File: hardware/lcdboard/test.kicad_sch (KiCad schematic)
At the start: 29 parts, among them J1 Conn_02x16_Odd_Even_MountingP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, J2 Conn_01x45_Shielded, J3 CapTouch, U1 74CBTLV3257, U2 AP2502

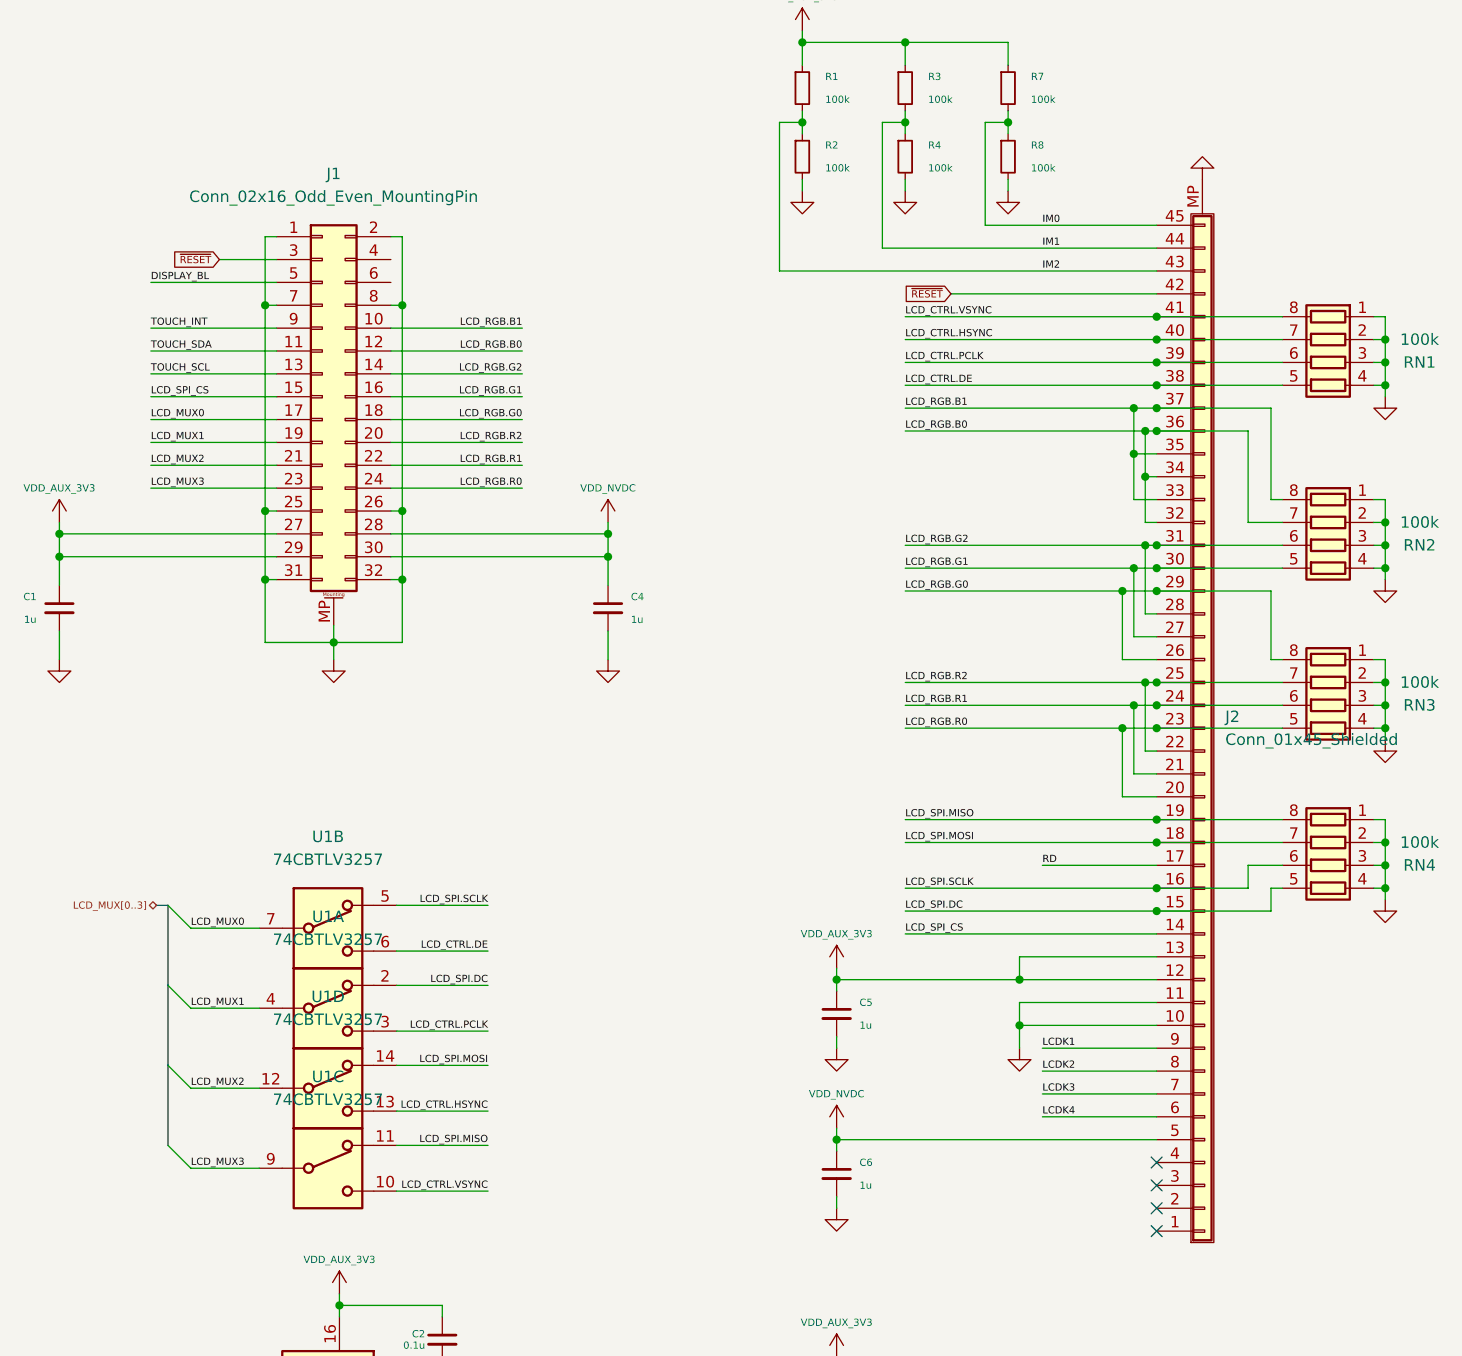
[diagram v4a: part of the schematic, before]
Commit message: completed layout for lcdboard prototype, may need to move b2b down for clearance on mainboard.
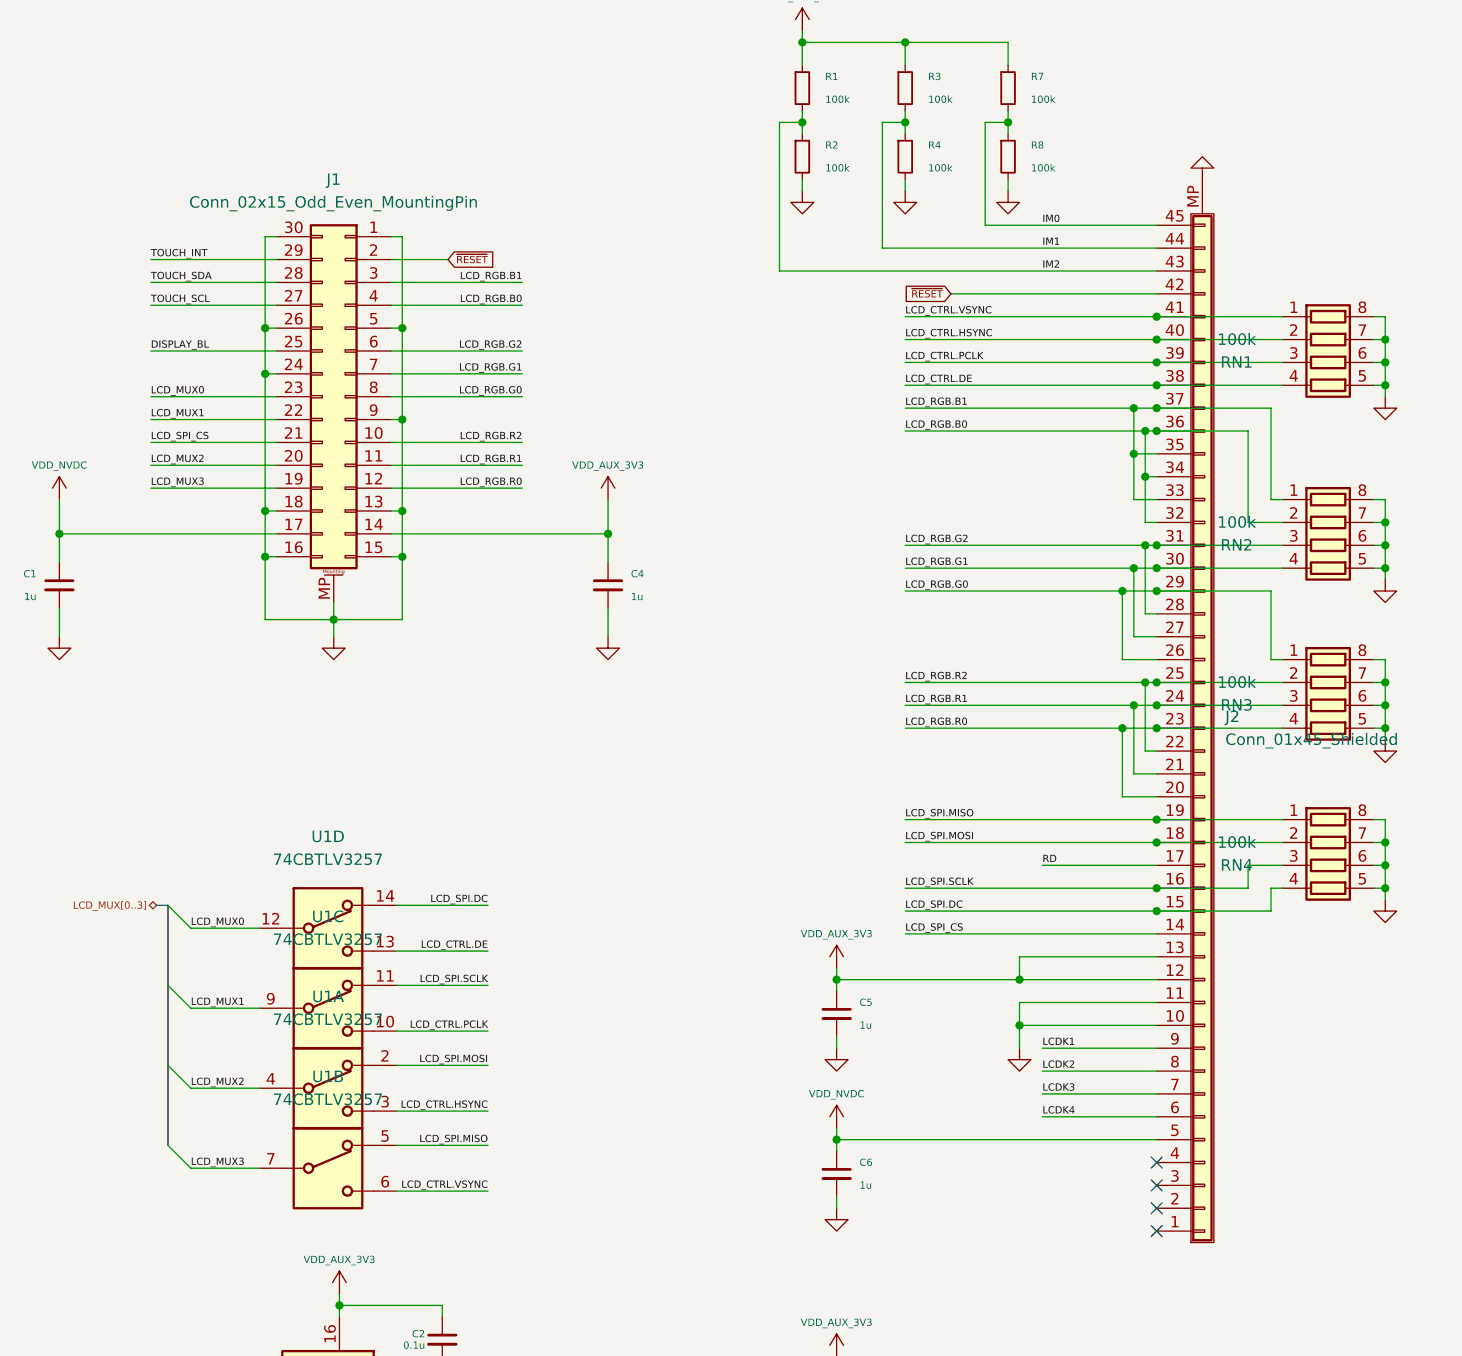
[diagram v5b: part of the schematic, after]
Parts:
- J1: value Conn_02x16_Odd_Even_MountingPin -> Conn_02x15_Odd_Even_MountingPin; footprint Connector_Molex:Molex_SlimStack_502426-3210_2x16_P0.40mm_Vertical -> bt_Connector_B2B:10132798-031100LF; symbol Connector_Generic_MountingPin:Conn_02x16_Odd_Even_MountingPin -> Connector_Generic_MountingPin:Conn_02x15_Counter_Clockwise_MountingPin
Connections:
- net DISPLAY_BL: now also J1.25 (Pin_25); no longer J1.5 (Pin_5)
- net GND: now also J1.13 (Pin_13), J1.15 (Pin_15), J1.16 (Pin_16), J1.18 (Pin_18), J1.24 (Pin_24), J1.30 (Pin_30), J1.5 (Pin_5), J1.9 (Pin_9), RN1.5 (R4.2), RN1.6 (R3.2), RN1.7 (R2.2), RN1.8 (R1.2), RN2.5 (R4.2), RN2.6 (R3.2), RN2.7 (R2.2), RN2.8 (R1.2), RN3.5 (R4.2), RN3.6 (R3.2), RN3.7 (R2.2), RN3.8 (R1.2), RN4.5 (R4.2), RN4.6 (R3.2), RN4.7 (R2.2), RN4.8 (R1.2); no longer J1.2 (Pin_2), J1.25 (Pin_25), J1.31 (Pin_31), J1.32 (Pin_32), J1.7 (Pin_7), J1.8 (Pin_8), RN1.1 (R1.1), RN1.2 (R2.1), RN1.3 (R3.1), RN1.4 (R4.1), RN2.1 (R1.1), RN2.2 (R2.1), RN2.3 (R3.1), RN2.4 (R4.1), RN3.1 (R1.1), RN3.2 (R2.1), RN3.3 (R3.1), RN3.4 (R4.1), RN4.1 (R1.1), RN4.2 (R2.1), RN4.3 (R3.1), RN4.4 (R4.1)
- net LCD_CTRL.DE: now also RN1.4 (R4.1), U1.13; no longer RN1.5 (R4.2), U1.6
- net LCD_CTRL.HSYNC: now also RN1.2 (R2.1), U1.3; no longer RN1.7 (R2.2), U1.13
- net LCD_CTRL.PCLK: now also RN1.3 (R3.1), U1.10; no longer RN1.6 (R3.2), U1.3
- net LCD_CTRL.VSYNC: now also RN1.1 (R1.1), U1.6; no longer RN1.8 (R1.2), U1.10
- net LCD_MUX0: now also J1.23 (Pin_23), U1.12; no longer J1.17 (Pin_17), U1.7
- net LCD_MUX1: now also J1.22 (Pin_22), U1.9; no longer J1.19 (Pin_19), U1.4
- net LCD_MUX2: now also J1.20 (Pin_20), U1.4; no longer J1.21 (Pin_21), U1.12
- net LCD_MUX3: now also J1.19 (Pin_19), U1.7; no longer J1.23 (Pin_23), U1.9
- net LCD_RGB.B0: now also J1.4 (Pin_4), RN2.2 (R2.1); no longer J1.12 (Pin_12), RN2.7 (R2.2)
- net LCD_RGB.B1: now also J1.3 (Pin_3), RN2.1 (R1.1); no longer J1.10 (Pin_10), RN2.8 (R1.2)
- net LCD_RGB.G0: now also J1.8 (Pin_8), RN3.1 (R1.1); no longer J1.18 (Pin_18), RN3.8 (R1.2)
- net LCD_RGB.G1: now also J1.7 (Pin_7), RN2.4 (R4.1); no longer J1.16 (Pin_16), RN2.5 (R4.2)
- net LCD_RGB.G2: now also J1.6 (Pin_6), RN2.3 (R3.1); no longer J1.14 (Pin_14), RN2.6 (R3.2)
- net LCD_RGB.R0: now also J1.12 (Pin_12), RN3.4 (R4.1); no longer J1.24 (Pin_24), RN3.5 (R4.2)
- net LCD_RGB.R1: now also J1.11 (Pin_11), RN3.3 (R3.1); no longer J1.22 (Pin_22), RN3.6 (R3.2)
- net LCD_RGB.R2: now also J1.10 (Pin_10), RN3.2 (R2.1); no longer J1.20 (Pin_20), RN3.7 (R2.2)
- net LCD_SPI.DC: now also RN4.4 (R4.1), U1.14; no longer RN4.5 (R4.2), U1.2
- net LCD_SPI.MISO: now also RN4.1 (R1.1), U1.5; no longer RN4.8 (R1.2), U1.11
- net LCD_SPI.MOSI: now also RN4.2 (R2.1), U1.2; no longer RN4.7 (R2.2), U1.14
- net LCD_SPI.SCLK: now also RN4.3 (R3.1), U1.11; no longer RN4.6 (R3.2), U1.5
- net LCD_SPI_CS: now also J1.21 (Pin_21); no longer J1.15 (Pin_15)
- net TOUCH_INT: now also J1.29 (Pin_29); no longer J1.9 (Pin_9)
- net TOUCH_SCL: now also J1.27 (Pin_27); no longer J1.13 (Pin_13)
- net TOUCH_SDA: now also J1.28 (Pin_28); no longer J1.11 (Pin_11)
- net VDD_AUX_3V3: now also C4.1, J1.14 (Pin_14); no longer C1.1, J1.27 (Pin_27), J1.29 (Pin_29)
- net VDD_NVDC: now also C1.1, J1.17 (Pin_17); no longer C4.1, J1.28 (Pin_28), J1.30 (Pin_30)
- net ~{RESET}: now also J1.2 (Pin_2); no longer J1.3 (Pin_3)
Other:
- moved on the sheet: C1, C4, RN1, RN2, RN3, RN4, U1A, U1B, U1C, U1D

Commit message: relayout screen
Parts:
- removed C1, C4: 1u, Capacitor_SMD:C_0603_1608Metric, symbol Device:C_Small
- added C3, C8: 1u, Capacitor_SMD:C_0603_1608Metric, symbol Device:C_Small
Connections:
- net DISPLAY_BL: now also J1.20 (Pin_20); no longer J1.25 (Pin_25)
- net GND: now also J1.12 (Pin_12), J1.27 (Pin_27), J1.4 (Pin_4), J1.8 (Pin_8), C3.2, C8.2; no longer H1.1, H2.1, H3.1, H4.1, J1.13 (Pin_13), J1.18 (Pin_18), J1.24 (Pin_24), J1.26 (Pin_26), J1.5 (Pin_5), J1.9 (Pin_9)
- net LCD_CTRL.DE: now also U1.3; no longer U1.13
- net LCD_CTRL.HSYNC: now also U1.10; no longer U1.3
- net LCD_CTRL.PCLK: now also U1.6; no longer U1.10
- net LCD_CTRL.VSYNC: now also U1.13; no longer U1.6
- net LCD_MUX0: now also J1.21 (Pin_21); no longer J1.23 (Pin_23)
- net LCD_MUX2: now also J1.23 (Pin_23), U1.7; no longer J1.20 (Pin_20), U1.4
- net LCD_MUX3: now also J1.24 (Pin_24), U1.4; no longer J1.19 (Pin_19), U1.7
- net LCD_RGB.B0: now also J1.3 (Pin_3); no longer J1.4 (Pin_4)
- net LCD_RGB.B1: now also J1.2 (Pin_2); no longer J1.3 (Pin_3)
- net LCD_RGB.G0: now also J1.7 (Pin_7); no longer J1.8 (Pin_8)
- net LCD_RGB.G1: now also J1.6 (Pin_6); no longer J1.7 (Pin_7)
- net LCD_RGB.G2: now also J1.5 (Pin_5); no longer J1.6 (Pin_6)
- net LCD_RGB.R0: now also J1.11 (Pin_11); no longer J1.12 (Pin_12)
- net LCD_RGB.R1: now also J1.10 (Pin_10); no longer J1.11 (Pin_11)
- net LCD_RGB.R2: now also J1.9 (Pin_9); no longer J1.10 (Pin_10)
- net LCD_SPI.DC: now also U1.2; no longer U1.14
- net LCD_SPI.MISO: now also U1.14; no longer U1.5
- net LCD_SPI.MOSI: now also U1.11; no longer U1.2
- net LCD_SPI.SCLK: now also U1.5; no longer U1.11
- net LCD_SPI_CS: now also J1.25 (Pin_25); no longer J1.21 (Pin_21)
- net TOUCH_INT: now also J1.19 (Pin_19); no longer J1.29 (Pin_29)
- net TOUCH_SCL: now also J1.17 (Pin_17); no longer J1.27 (Pin_27)
- net TOUCH_SDA: now also J1.18 (Pin_18); no longer J1.28 (Pin_28)
- net VDD_AUX_3V3: now also C6.1, J1.13 (Pin_13), J1.28 (Pin_28), J1.29 (Pin_29), J2.5 (Pin_5), C3.1, C8.1
- net ~{RESET}: now also J1.26 (Pin_26); no longer J1.2 (Pin_2)
- removed net VDD_NVDC: C6.1, J1.17 (Pin_17), J2.5 (Pin_5)
- no-connect marks 4 -> 8
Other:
- moved on the sheet: U1A, U1B
